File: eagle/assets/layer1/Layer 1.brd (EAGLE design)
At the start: 196 x 185.9 mm, 246 parts, among them M1C1 33nF, M1C2 680uF, M1C3 1.0uF, M1D1 RED, M1D2 BLUE, M1J1 XT30PB-F, M1Q1 AOD482, M1R1 1k, M1R10 1k, M1R11 10k, M1R12 4.7k, M1R2 1k, M1R3 3.3k, M1R4 3.3k, M1R5 1k, M1R6 1k, M1R7 1k, M1R8 10k, M1R9 10k, M2C1 33nF, M2C2 680uF, M2C3 1.0uF, M2D1 RED, M2D2 BLUE, M2J1 XT30PB-F, M2Q1 AOD482, M2R1 1k, M2R10 1k, M2R11 10k, M2R12 4.7k, M2R2 1k, M2R3 3.3k, M2R4 3.3k, M2R5 1k, M2R6 1k, M2R7 1k, M2R8 10k, M2R9 10k, M3C1 33nF, M3C2 680uF, M3C3 1.0uF, M3D1 RED, M3D2 BLUE, M3J1 XT30PB-F, M3Q1 AOD482, M3R1 1k, M3R10 1k, M3R11 10k, M3R12 4.7k, M3R2 1k, M3R3 3.3k, M3R4 3.3k, M3R5 1k, M3R6 1k, M3R7 1k, M3R8 10k, M3R9 10k, M4C1 33nF, M4C2 680uF, M4C3 1.0uF, M4D1 RED, M4D2 BLUE, M4J1 XT30PB-F, M4Q1 AOD482, M4R1 1k, M4R10 1k, M4R11 10k, M4R12 4.7k, M4R2 1k, M4R3 3.3k, M4R4 3.3k, M4R5 1k, M4R6 1k, M4R7 1k, M4R8 10k, M4R9 10k, Q37 AO3402, X2 SM06B-SRSS-TB, Y1 8MHz

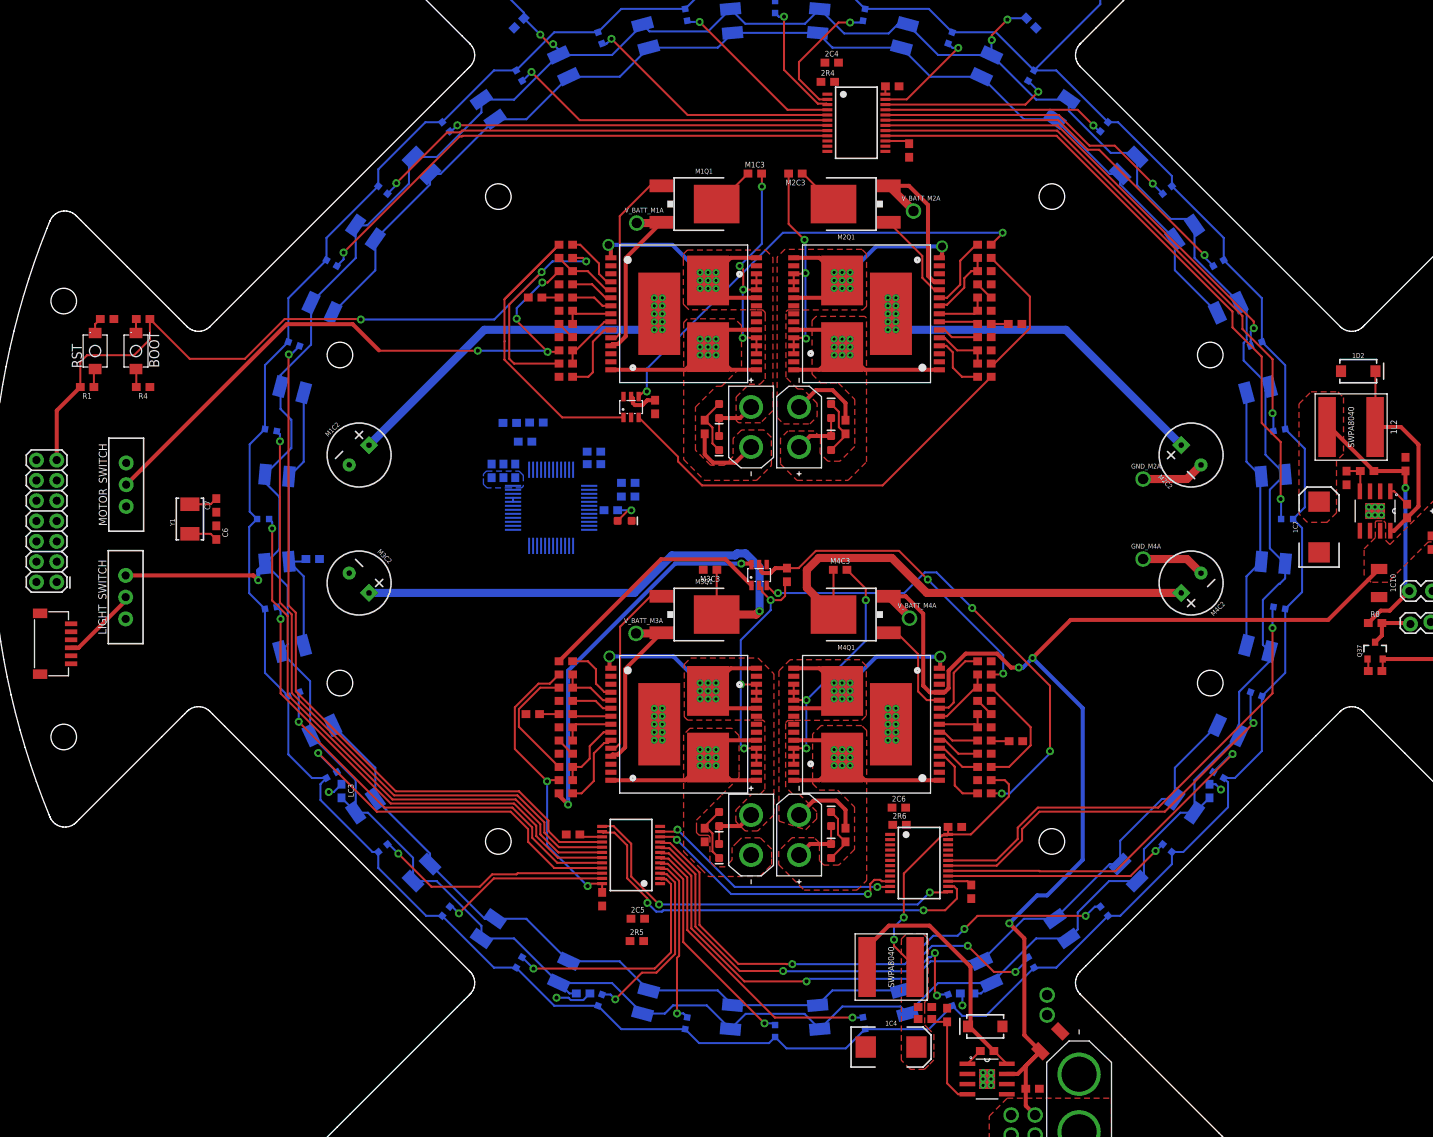
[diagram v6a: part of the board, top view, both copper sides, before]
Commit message: routed some to STEM32
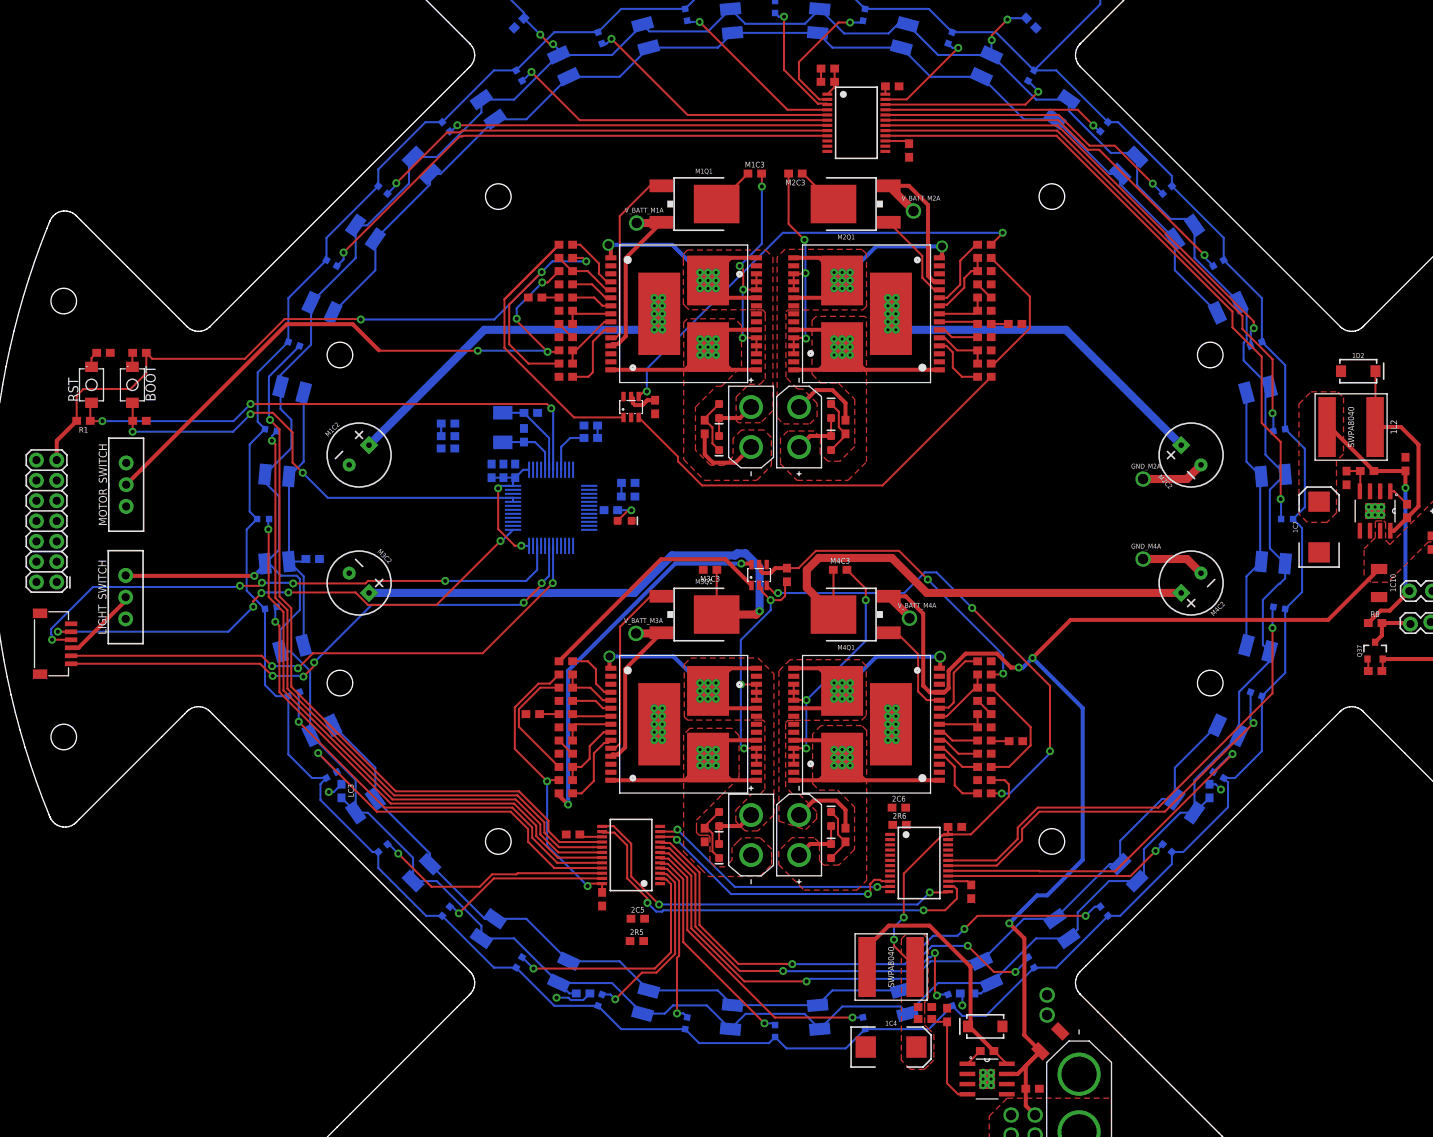
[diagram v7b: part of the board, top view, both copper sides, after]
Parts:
- moved C7 41.0 mm to (-30.5, 13.3), flipped to the bottom, turned to 0 degrees
- moved Y1 40.8 mm to (-34.0, 11.4), flipped to the bottom
- moved C6 40.3 mm to (-31.4, 10.5), flipped to the bottom
- moved C5 11.1 mm to (-40.9, 11.9)
- moved FB2 9.67 mm to (-40.9, 8.83), turned to 180 degrees
- moved C4 7.89 mm to (-40.9, 10.4)
- moved BOOT 4.25 mm to (-80.3, 16.8)
- moved R1 4.25 mm to (-86.4, 12.3)
- moved R2 4.25 mm to (-83.9, 20.8)
- moved R3 4.25 mm to (-79.4, 20.8)
- moved R4 4.25 mm to (-79.4, 12.3)
- moved RST 4.25 mm to (-85.4, 16.8)
- moved FB1 3.30 mm to (-23.0, 10.1)
- moved C8 3.29 mm to (-23.0, 11.7)
- moved 2C4 0.89 mm to (6.59, 56.3), turned to 180 degrees
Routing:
- net SWDIO: track 0.00 -> 70.7 mm, vias 0 -> 5
- net TX1: track 0.00 -> 69.9 mm, vias 0 -> 3
- net RX1: track 0.00 -> 69.7 mm, vias 0 -> 5
- net RESET: track 2.31 -> 68.8 mm, vias 0 -> 3
- net SWCLK: track 0.00 -> 65.5 mm, vias 0 -> 5
- net BOOT0: track 2.77 -> 59.3 mm, vias 0 -> 3
- net 3.3V: track 255.7 -> 268.6 mm, vias 9 -> 11
- net VCCA: track 464.2 -> 473.8 mm
- net OSC_OUT: track 3.59 -> 11.1 mm
- net OSC_IN: track 3.59 -> 10.8 mm
- net LSIG1: track 0.00 -> 3.58 mm
- net LSWITCH: track 502.1 -> 504.5 mm
- net N$83: track 91.1 -> 93.0 mm
- net BATT_LVL: track 0.00 -> 1.71 mm
- net AGND: track 0.00 -> 1.66 mm
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- removed copper zone on layer 16, net 3.3V

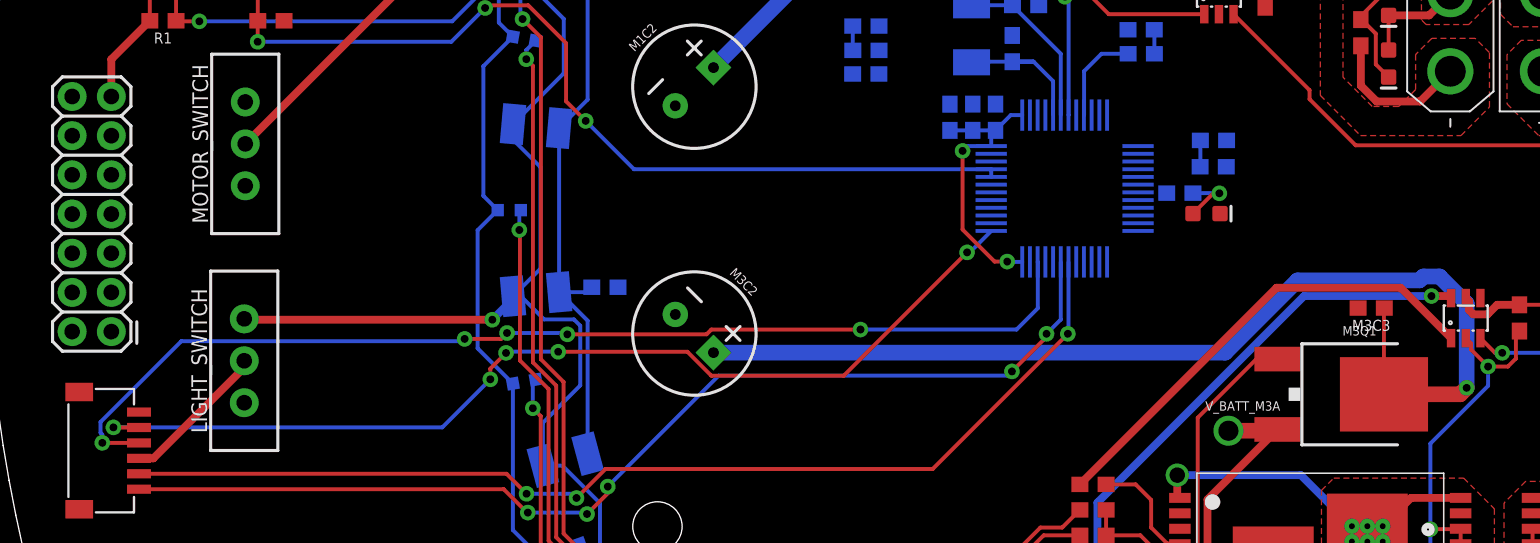
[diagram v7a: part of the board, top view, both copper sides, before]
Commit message: routed some to STEM32
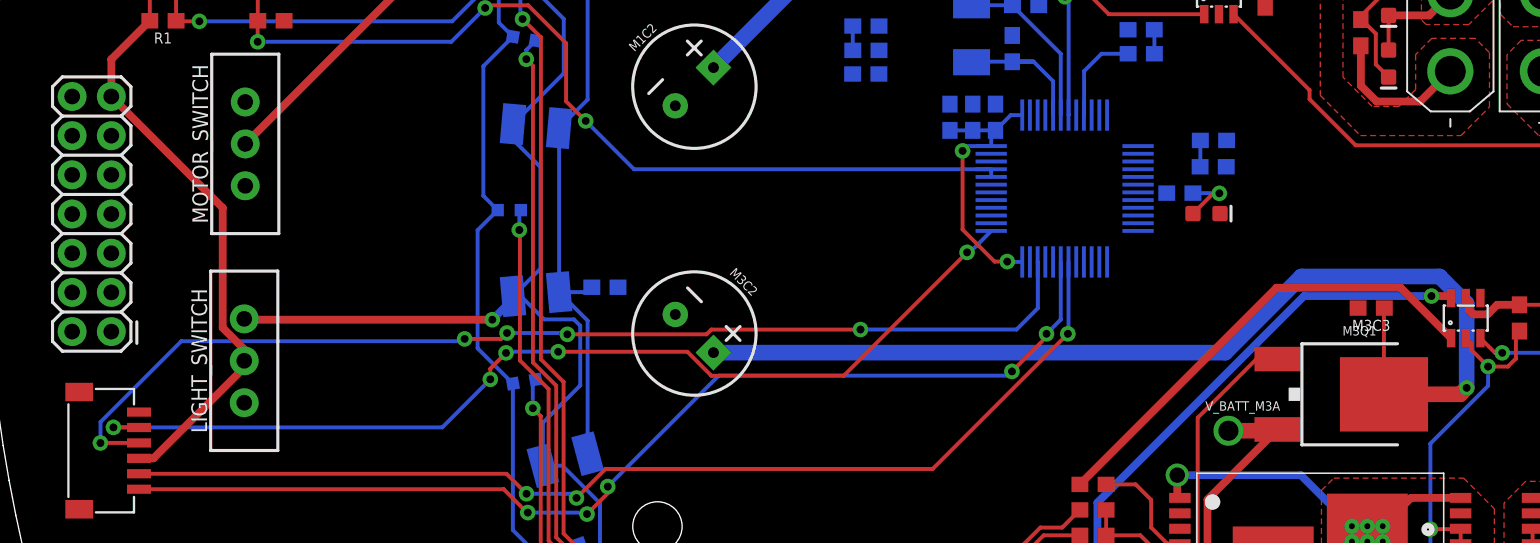
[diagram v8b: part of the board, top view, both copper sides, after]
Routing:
- net 3.3V: track 268.6 -> 289.3 mm
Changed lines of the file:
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@@
 <wire x1="-32.542459375" y1="-3.33501875" x2="-34.6169875" y2="-1.260490625" width="0.254" layer="1"/>
 <wire x1="-34.6169875" y1="-1.260490625" x2="-34.6169875" y2="3.837915625" width="0.254" layer="1"/>
-<wire x1="-89.79408125" y1="7.366" x2="-81.1784" y2="-9.766296875" width="0" layer="19" extent="1-1"/>
-<wire x1="-22.190665625" y1="11.690146875" x2="-27.012" y2="19.431" width="0" layer="19" extent="1-16"/>
+<wire x1="-81.1784" y1="-9.02415625" x2="-81.1784" y2="-9.766296875" width="0.508" layer="1"/>
+<wire x1="-82.5754" y1="-7.62715625" x2="-81.1784" y2="-9.02415625" width="0.508" layer="1"/>
+<wire x1="-89.79408125" y1="7.366" x2="-82.5754" y2="0.14731875" width="0.508" layer="1"/>
+<wire x1="-82.5754" y1="0.14731875" x2="-82.5754" y2="-7.62715625" width="0.508" layer="1"/>
+<wire x1="27.012" y1="32.639" x2="13.785" y2="53.105" width="0" layer="19" extent="1-1"/>
+<wire x1="19.08696875" y1="-7.5627125" x2="27.012" y2="19.431" width="0" layer="19" extent="1-1"/>
+<wire x1="27.012" y1="-32.639" x2="27.012" y2="-19.431" width="0" layer="19" extent="1-1"/>
+<wire x1="17.881334375" y1="-61" x2="17.5" y2="-56" width="0" layer="19" extent="1-1"/>
+<wire x1="17.881334375" y1="-62.5" x2="17.881334375" y2="-61" width="0" layer="19" extent="1-1"/>
+<wire x1="17.67" y1="-66" x2="17.881334375" y2="-62.5" width="0" layer="19" extent="1-1"/>
+<wire x1="-23.242" y1="-1.35" x2="-2" y2="-5.7" width="0" layer="19" extent="1-16"/>
+<wire x1="-30.75" y1="-3.358" x2="-23.242" y2="-1.35" width="0" layer="19" extent="16-16"/>
+<wire x1="-22.183196875" y1="10.133921875" x2="-30.75" y2="6.158" width="0" layer="19" extent="16-16"/>
 <wire x1="-18" y1="15.3" x2="-22.190665625" y2="11.690146875" width="0" layer="19" extent="1-16"/>
-<wire x1="-30.75" y1="6.158" x2="-22.183196875" y2="10.133921875" width="0" layer="19" extent="16-16"/>
-<wire x1="-23.242" y1="-1.35" x2="-30.75" y2="-3.358" width="0" layer="19" extent="16-16"/>
+<wire x1="-27.012" y1="19.431" x2="-22.190665625" y2="11.690146875" width="0" layer="19" extent="1-16"/>
 <wire x1="-27.012" y1="-19.431" x2="-30.75" y2="-3.358" width="0" layer="19" extent="1-16"/>
-<wire x1="-2" y1="-5.7" x2="-23.242" y2="-1.35" width="0" layer="19" extent="1-16"/>
-<wire x1="27.012" y1="-32.639" x2="27.012" y2="-19.431" width="0" layer="19" extent="1-1"/>
-<wire x1="27.012" y1="19.431" x2="19.08696875" y2="-7.5627125" width="0" layer="19" extent="1-1"/>
-<wire x1="13.785" y1="53.105" x2="27.012" y2="32.639" width="0" layer="19" extent="1-1"/>
 </signal>
 <signal name="LSWITCH">
@@
 <wire x1="-2.35711875" y1="-11.938" x2="-1.940559375" y2="-11.521440625" width="1.016" layer="1"/>
 <via x="-1.940559375" y="-11.521440625" extent="1-16" drill="0.508"/>
-<wire x1="-3.695425" y1="-4.30021875" x2="-4.7475375" y2="-4.30021875" width="1.016" layer="16"/>
-<wire x1="-4.7475375" y1="-4.30021875" x2="-5.0015375" y2="-4.55421875" width="1.016" layer="16"/>
 <wire x1="-1.940559375" y1="-11.521440625" x2="-1.940559375" y2="-6.055084375" width="1.016" layer="16"/>
 <wire x1="-1.940559375" y1="-6.055084375" x2="-3.695425" y2="-4.30021875" width="1.016" layer="16"/>
 <wire x1="-17.588159375" y1="-9.237434375" x2="-50.7625625" y2="-9.237434375" width="1.016" layer="16"/>
-<wire x1="-5.0015375" y1="-4.55421875" x2="-12.90494375" y2="-4.55421875" width="1.016" layer="16"/>
-<wire x1="-12.90494375" y1="-4.55421875" x2="-17.588159375" y2="-9.237434375" width="1.016" layer="16"/>
+<wire x1="-3.695425" y1="-4.30021875" x2="-12.65094375" y2="-4.30021875" width="1.016" layer="16"/>
+<wire x1="-12.65094375" y1="-4.30021875" x2="-17.588159375" y2="-9.237434375" width="1.016" layer="16"/>
 <wire x1="-7.302" y1="-11.938" x2="-14.099" y2="-23.654" width="0" layer="19" extent="1-1"/>
 </signal>
@@
 <contactref element="U$2" pad="34"/>
 <contactref element="X2" pad="3"/>
-<wire x1="-88" y1="-15.090521875" x2="-90.374909375" y2="-15.090521875" width="0.254" layer="1"/>
-<wire x1="-90.374909375" y1="-15.090521875" x2="-90.379328125" y2="-15.086103125" width="0.254" layer="1"/>
-<via x="-90.379328125" y="-15.086103125" extent="1-16" drill="0.508"/>
-<wire x1="-90.49511875" y1="-14.4315" x2="-90.49511875" y2="-13.7371" width="0.254" layer="16"/>
-<wire x1="-90.379328125" y1="-15.086103125" x2="-90.379328125" y2="-14.547290625" width="0.254" layer="16"/>
-<wire x1="-90.379328125" y1="-14.547290625" x2="-90.49511875" y2="-14.4315" width="0.254" layer="16"/>
+<wire x1="-88" y1="-15.090521875" x2="-90.4976125" y2="-15.090521875" width="0.254" layer="1"/>
+<wire x1="-90.4976125" y1="-15.090521875" x2="-90.502453125" y2="-15.0953625" width="0.254" layer="1"/>
+<via x="-90.502453125" y="-15.0953625" extent="1-16" drill="0.508"/>
+<wire x1="-90.49511875" y1="-13.7371" x2="-90.49511875" y2="-15.088028125" width="0.254" layer="16"/>
+<wire x1="-90.502453125" y1="-15.0953625" x2="-90.49511875" y2="-15.088028125" width="0.254" layer="16"/>
 <wire x1="-90.49511875" y1="-13.7371" x2="-85.2543125" y2="-8.49629375" width="0.254" layer="16"/>
 <wire x1="-85.2543125" y1="-8.49629375" x2="-67.0391875" y2="-8.49629375" width="0.254" layer="16"/>
@@
 <contactref element="U$2" pad="22"/>
 <contactref element="U$15" pad="11"/>
-<wire x1="-23.242" y1="-0.35" x2="-89.79408125" y2="4.826" width="0" layer="19" extent="16-16"/>
+<wire x1="-89.79408125" y1="4.826" x2="-23.242" y2="-0.35" width="0" layer="19" extent="16-16"/>
 </signal>
 <signal name="LIGHT_INT">
